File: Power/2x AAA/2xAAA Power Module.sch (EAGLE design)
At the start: 3 parts

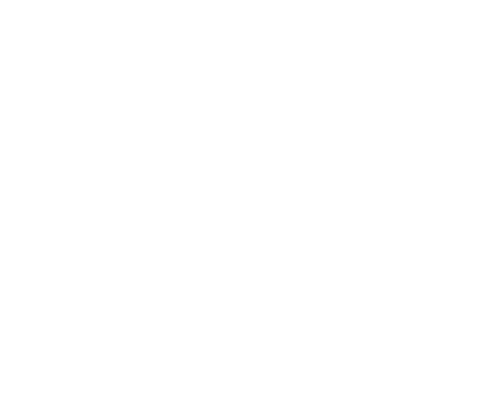
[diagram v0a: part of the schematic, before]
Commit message: Trying out different connectors
Signed-off-by: Cruz Monrreal II <Cruz.Monrreal@gmail.com>
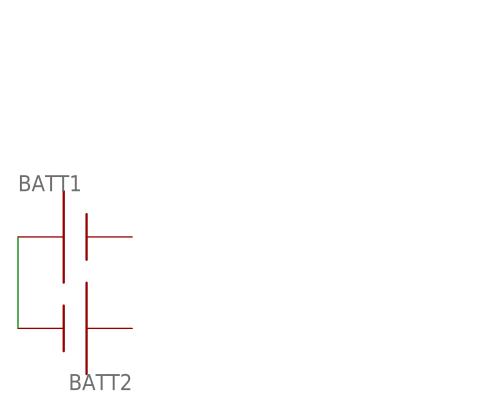
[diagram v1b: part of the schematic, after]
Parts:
- added BATT1, BATT2: AAA, adafruit:AAA
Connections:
- new net N$16: BATT1.-, BATT2.+
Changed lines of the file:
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@@
 <part name="U$3" library=".screw_holes" deviceset="HOLE" device=".2MM"/>
 <part name="U$8" library="thinkmaketest" deviceset="ROOT1" device=".BOTH"/>
+<part name="BATT1" library="adafruit" deviceset="AAA" device=""/>
+<part name="BATT2" library="adafruit" deviceset="AAA" device=""/>
 </parts>
 <sheets>
@@
 <instance part="U$8" gate="G$1" x="172.72" y="111.76"/>
 <instance part="U$8" gate="G$2" x="210.82" y="127"/>
+<instance part="BATT1" gate="G$1" x="104.14" y="93.98"/>
+<instance part="BATT2" gate="G$1" x="101.6" y="83.82" rot="R180"/>
 </instances>
 <busses>
@@
 </segment>
 </net>
+<net name="N$16" class="0">
+<segment>
+<pinref part="BATT2" gate="G$1" pin="+"/>
+<pinref part="BATT1" gate="G$1" pin="-"/>
+<wire x1="96.52" y1="83.82" x2="96.52" y2="93.98" width="0.1524" layer="91"/>
+</segment>
+</net>

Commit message: Added note as to which connectors to use
Signed-off-by: Cruz Monrreal II <Cruz.Monrreal@gmail.com>
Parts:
- removed BATT1, BATT2: AAA, adafruit:AAA
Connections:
- removed net N$16: BATT1.-, BATT2.+
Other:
- note added: "Use #55 from http://www.keyelco.com/pdfs/M60/M60p8.pdf"
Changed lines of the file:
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@@
 <part name="U$3" library=".screw_holes" deviceset="HOLE" device=".2MM"/>
 <part name="U$8" library="thinkmaketest" deviceset="ROOT1" device=".BOTH"/>
-<part name="BATT1" library="adafruit" deviceset="AAA" device=""/>
-<part name="BATT2" library="adafruit" deviceset="AAA" device=""/>
 </parts>
 <sheets>
 <sheet>
 <plain>
+<text x="10.16" y="71.12" size="5.08" layer="97">Use #55 from http://www.keyelco.com/pdfs/M60/M60p8.pdf</text>
 </plain>
 <instances>
@@
 <instance part="U$8" gate="G$1" x="172.72" y="111.76"/>
 <instance part="U$8" gate="G$2" x="210.82" y="127"/>
-<instance part="BATT1" gate="G$1" x="104.14" y="93.98"/>
-<instance part="BATT2" gate="G$1" x="101.6" y="83.82" rot="R180"/>
 </instances>
 <busses>
@@
 </segment>
 </net>
-<net name="N$16" class="0">
-<segment>
-<pinref part="BATT2" gate="G$1" pin="+"/>
-<pinref part="BATT1" gate="G$1" pin="-"/>
-<wire x1="96.52" y1="83.82" x2="96.52" y2="93.98" width="0.1524" layer="91"/>
-</segment>
-</net>
